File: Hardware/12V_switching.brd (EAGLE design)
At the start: 39.4 x 50.9 mm, 10 parts, among them IC5 LM2576D2TR4-012G, J1 POWERPOLE_POWER45A, J2 POWERPOLE_POWER45A

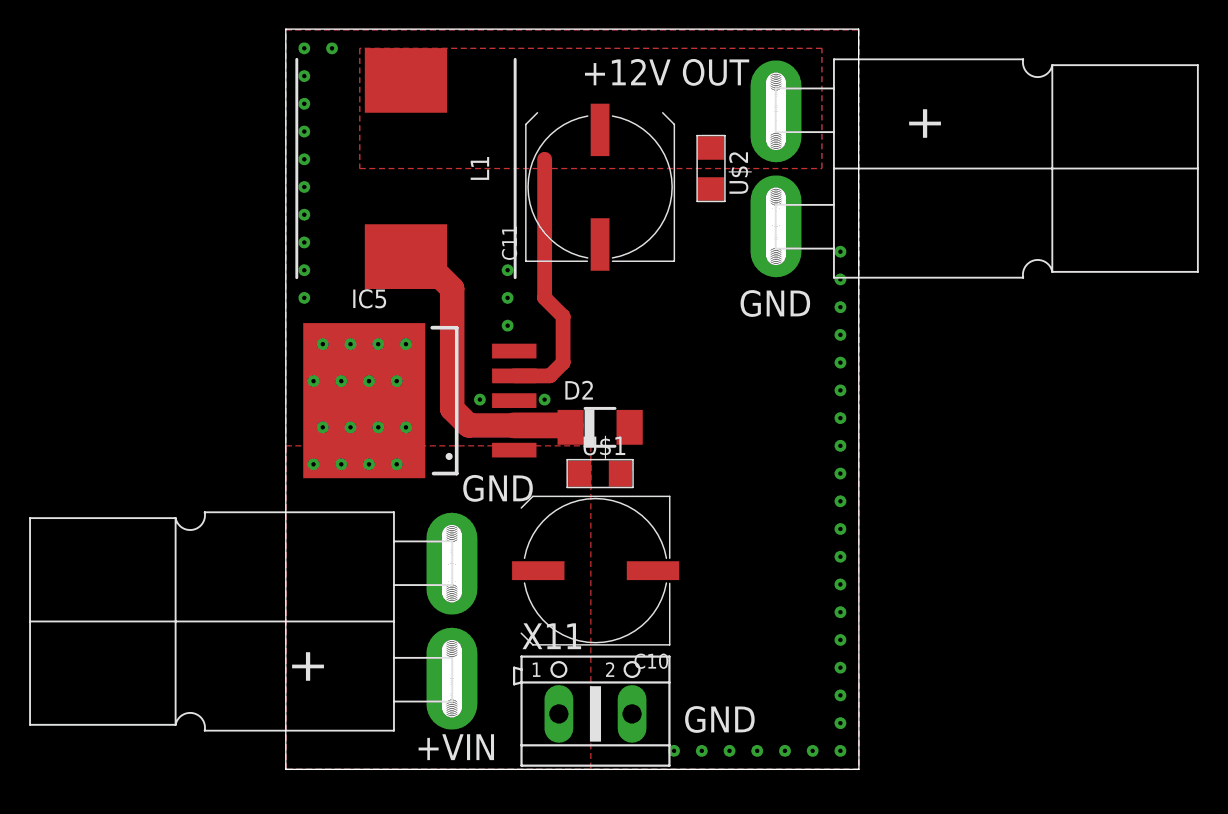
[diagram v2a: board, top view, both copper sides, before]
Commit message: Fix dimention layer on  RTI-Dome-eth.brd, added MPN on all component for mouser.
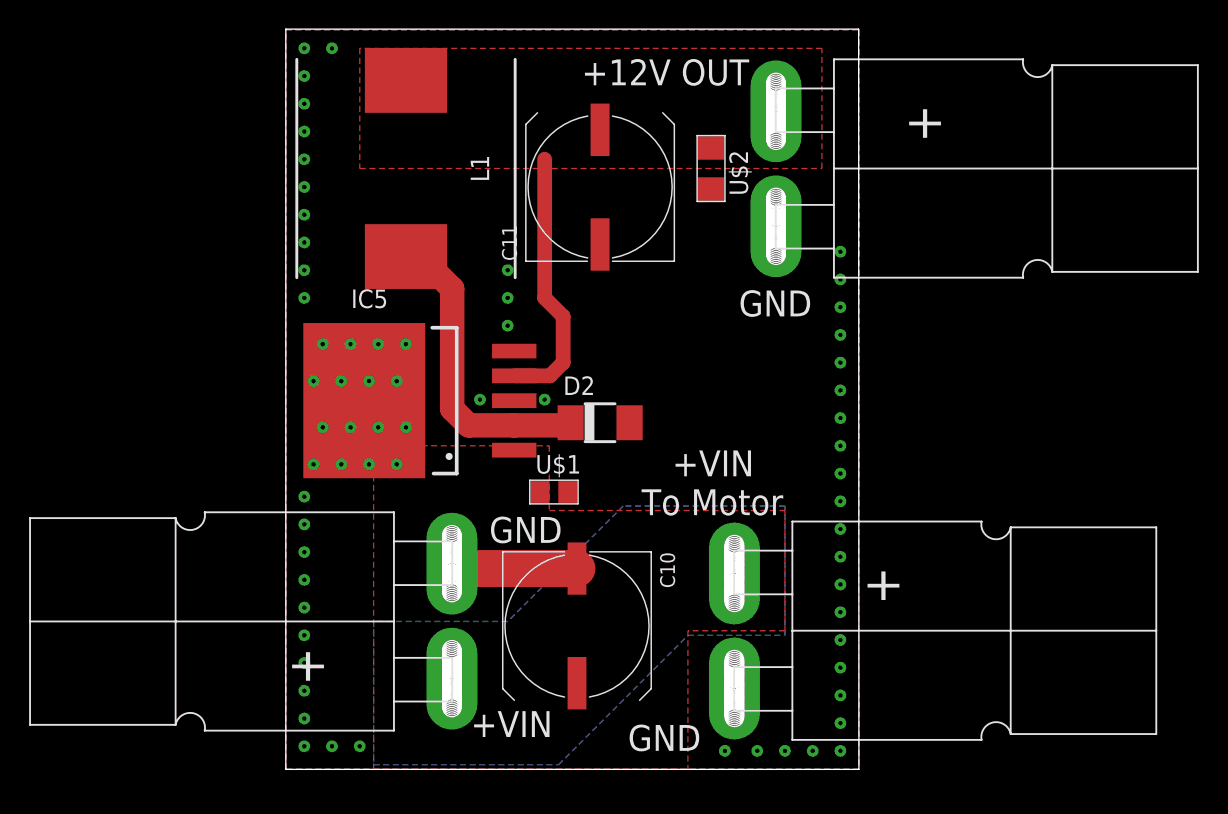
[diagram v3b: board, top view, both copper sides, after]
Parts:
- removed X11: (no value), con-ptr500:AK500/2
- added J3: POWERPOLE_POWER45A, powerpoles:POWERPOLE_PAIR_45A
- U$1: device rti:C1206 -> rti:C0805
- moved C10 4.02 mm to (20.0, 9.84), turned to 270 degrees
- moved U$1 3.42 mm to (18.4, 19.1)
- moved D2 0.32 mm to (21.6, 23.8)
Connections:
- new net V+: J3.RED
- net +VIN: no longer X11.1
- net GND: now also J3.BLACK; no longer X11.2
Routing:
- net GND: track 0.00 -> 8.93 mm, vias 57 -> 67
- added copper zone on layer 16, net +VIN
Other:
- board text added: "+VIN To Motor"
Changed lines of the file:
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@@
 <wire x1="39.35" y1="50.851" x2="0" y2="50.851" width="0" layer="20"/>
 <wire x1="0" y1="50.851" x2="0" y2="0" width="0" layer="20"/>
-<text x="8.89" y="0.635" size="1.778" layer="25">+VIN</text>
-<text x="12.065" y="18.415" size="1.778" layer="25">GND</text>
+<text x="12.7" y="2.2225" size="1.778" layer="25">+VIN</text>
+<text x="13.97" y="15.5575" size="1.778" layer="25">GND</text>
 <text x="31.115" y="31.115" size="1.778" layer="25">GND</text>
 <text x="20.32" y="46.99" size="1.778" layer="25">+12V OUT</text>
-<text x="27.305" y="2.54" size="1.778" layer="25">GND</text>
+<text x="23.495" y="1.27" size="1.778" layer="25">GND</text>
+<text x="24.4475" y="17.4625" size="1.778" layer="21">   +VIN
+To Motor</text>
 </plain>
 <attributes>
@@
 </autorouter>
 <elements>
-<element name="C10" library="rcl" package="UD-10X10_NICHICON" value="100uF" x="21.2725" y="13.6525" rot="R180"/>
+<element name="C10" library="rcl" package="UD-10X10_NICHICON" value="100uF" x="20.0025" y="9.8425" rot="R270"/>
 <element name="C11" library="rcl" package="UD-10X10_NICHICON" value="1000uF" x="21.59" y="40.005" rot="R90"/>
-<element name="D2" library="diode" package="DO-214AC" value="SAC32" x="21.59" y="23.495"/>
+<element name="D2" library="diode" package="DO-214AC" value="SAC32" x="21.59" y="23.8125"/>
 <element name="IC5" library="LM2576" package="TO263-5" value="LM2576D2TR4-012G" x="6.985" y="25.4" rot="R90">
 <attribute name="MOUSER_PART_NUMBER" value="863-LM2576D2TR4-012G" x="6.985" y="25.4" size="1.778" layer="27" rot="R90" display="off"/>
@@
 <attribute name="DESCRIPTION" value="Fixed Inductors MSS1583 SMT Power 0.103Ohms 100uH" x="8.255" y="41.275" size="1.778" layer="27" rot="R90" display="off"/>
 </element>
-<element name="U$1" library="rti" package="C1206" value="47uF" x="21.59" y="20.32"/>
+<element name="U$1" library="rti" package="C0805" value="47uF" x="18.415" y="19.05"/>
 <element name="U$2" library="rti" package="C1206" value="47uF" x="29.21" y="41.275" rot="R270"/>
 <element name="J1" library="powerpoles" package="POWERPOLE_PAIR_45A" value="POWERPOLE_POWER45A" x="11.43" y="10.16" rot="R90"/>
 <element name="J2" library="powerpoles" package="POWERPOLE_PAIR_45A" value="POWERPOLE_POWER45A" x="33.655" y="41.275" rot="R270"/>
-<element name="X11" library="con-ptr500" package="AK500/2" value="" x="21.2725" y="3.81">
-<attribute name="OC_NEWARK" value="unknown" x="21.2725" y="3.81" size="1.778" layer="27" display="off"/>
-<attribute name="MPN" value="" x="21.2725" y="3.81" size="1.778" layer="27" display="off"/>
-<attribute name="MF" value="" x="21.2725" y="3.81" size="1.778" layer="27" display="off"/>
-<attribute name="OC_FARNELL" value="unknown" x="21.2725" y="3.81" size="1.778" layer="27" display="off"/>
-</element>
+<element name="J3" library="powerpoles" package="POWERPOLE_PAIR_45A" value="POWERPOLE_POWER45A" x="30.7975" y="9.525" rot="R270"/>
 </elements>
 <signals>
@@
 <contactref element="D2" pad="A"/>
 <contactref element="C11" pad="-"/>
-<polygon width="0.4064" layer="16" thermals="no">
+<polygon width="0.4064" layer="16" thermals="no" rank="2">
 <vertex x="0" y="0"/>
 <vertex x="0" y="50.8"/>
@@
 <contactref element="J2" pad="BLACK"/>
 <contactref element="J1" pad="BLACK"/>
-<contactref element="X11" pad="2"/>
+<via x="3.175" y="1.5875" extent="1-16" drill="0.3" diameter="0.8128"/>
+<via x="5.08" y="1.5875" extent="1-16" drill="0.3" diameter="0.8128"/>
+<via x="30.1625" y="1.27" extent="1-16" drill="0.3" diameter="0.8128"/>
+<via x="32.385" y="1.27" extent="1-16" drill="0.3" diameter="0.8128"/>
 <via x="34.29" y="1.27" extent="1-16" drill="0.3" diameter="0.8128"/>
-<via x="32.385" y="1.27" extent="1-16" drill="0.3" diameter="0.8128"/>
-<via x="30.48" y="1.27" extent="1-16" drill="0.3" diameter="0.8128"/>
-<via x="28.575" y="1.27" extent="1-16" drill="0.3" diameter="0.8128"/>
-<via x="26.67" y="1.27" extent="1-16" drill="0.3" diameter="0.8128"/>
+<contactref element="J3" pad="BLACK"/>
+<wire x1="20.0025" y1="13.7925" x2="11.41" y2="13.7925" width="2.54" layer="1"/>
+<wire x1="11.41" y1="13.7925" x2="11.41" y2="14.13" width="2.54" layer="1"/>
+<via x="1.27" y="18.7325" extent="1-16" drill="0.3" diameter="0.8128"/>
+<via x="1.27" y="16.8275" extent="1-16" drill="0.3" diameter="0.8128"/>
+<via x="1.27" y="14.9225" extent="1-16" drill="0.3" diameter="0.8128"/>
+<via x="1.27" y="13.0175" extent="1-16" drill="0.3" diameter="0.8128"/>
+<via x="1.27" y="11.1125" extent="1-16" drill="0.3" diameter="0.8128"/>
+<via x="1.27" y="9.2075" extent="1-16" drill="0.3" diameter="0.8128"/>
+<via x="1.27" y="7.3025" extent="1-16" drill="0.3" diameter="0.8128"/>
+<via x="1.27" y="5.3975" extent="1-16" drill="0.3" diameter="0.8128"/>
+<via x="1.27" y="3.4925" extent="1-16" drill="0.3" diameter="0.8128"/>
+<via x="1.27" y="1.5875" extent="1-16" drill="0.3" diameter="0.8128"/>
 </signal>
 <signal name="+VIN" class="1">
@@
 <contactref element="C10" pad="+"/>
 <polygon width="0.4064" layer="1" thermals="no">
-<vertex x="0" y="22.225"/>
-<vertex x="20.955" y="22.225"/>
-<vertex x="20.955" y="0"/>
-<vertex x="0" y="0"/>
+<vertex x="6.0325" y="22.225"/>
+<vertex x="18.0975" y="22.225"/>
+<vertex x="18.0975" y="17.78"/>
+<vertex x="34.29" y="17.78"/>
+<vertex x="34.29" y="9.525"/>
+<vertex x="27.6225" y="9.525"/>
+<vertex x="27.6225" y="0"/>
+<vertex x="6.0325" y="0"/>
 </polygon>
 <contactref element="U$1" pad="1"/>
 <contactref element="J1" pad="RED"/>
-<contactref element="X11" pad="1"/>
+<polygon width="0.254" layer="16">
+<vertex x="34.29" y="18.0975"/>
+<vertex x="23.1775" y="18.0975"/>
+<vertex x="15.24" y="10.16"/>
+<vertex x="6.0325" y="10.16"/>
+<vertex x="6.0325" y="0.3175"/>
+<vertex x="18.7325" y="0.3175"/>
+<vertex x="27.6225" y="9.2075"/>
+<vertex x="34.29" y="9.2075"/>
+</polygon>
 </signal>
 <signal name="+12V">
@@
 <contactref element="D2" pad="C"/>
 <contactref element="L1" pad="1"/>
-<wire x1="15.695" y1="23.628" x2="19.565" y2="23.628" width="1.778" layer="1"/>
-<wire x1="19.565" y1="23.628" x2="19.565" y2="23.495" width="1.778" layer="1"/>
 <wire x1="15.695" y1="23.628" x2="12.567" y2="23.628" width="1.6764" layer="1"/>
 <wire x1="12.567" y1="23.628" x2="11.43" y2="24.765" width="1.6764" layer="1"/>
@@
 <wire x1="9.525" y1="34.925" x2="7.285" y2="34.925" width="1.6764" layer="1"/>
 <wire x1="7.285" y1="34.925" x2="8.255" y2="35.225" width="1.6764" layer="1"/>
+<wire x1="15.695" y1="23.628" x2="19.565" y2="23.628" width="1.6764" layer="1"/>
+<wire x1="19.565" y1="23.628" x2="19.565" y2="23.8125" width="1.6764" layer="1"/>
+</signal>
+<signal name="V+">
+<contactref element="J3" pad="RED"/>
 </signal>
 </signals>
@@
 </board>
 </drawing>
+<compatibility>
+<note version="6.3" minversion="6.2.2" severity="warning">
+Since Version 6.2.2 text objects can contain more than one line,
+which will not be processed correctly with this version.
+</note>
+</compatibility>
 </eagle>

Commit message: Change pin mode for better interrupt detection
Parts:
- removed U$1: 47uF, rti:C0805
- C10: value 100uF -> 100uF 100V
- D2: value SAC32 -> SAC34
- IC5: value LM2576D2TR4-012G -> LM2576HVSX-12/NOPB
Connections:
- net +VIN: no longer U$1.1
- net GND: no longer U$1.2
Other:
- board text added: "+VOUT To Motor"
- board text removed: "+VIN To Motor"
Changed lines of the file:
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@@
 <text x="20.32" y="46.99" size="1.778" layer="25">+12V OUT</text>
 <text x="23.495" y="1.27" size="1.778" layer="25">GND</text>
-<text x="24.4475" y="17.4625" size="1.778" layer="21">   +VIN
+<text x="27.6225" y="17.78" size="1.778" layer="21"> +VOUT
 To Motor</text>
 </plain>
@@
 </autorouter>
 <elements>
-<element name="C10" library="rcl" package="UD-10X10_NICHICON" value="100uF" x="20.0025" y="9.8425" rot="R270"/>
+<element name="C10" library="rcl" package="UD-10X10_NICHICON" value="100uF 100V" x="20.0025" y="9.8425" rot="R270"/>
 <element name="C11" library="rcl" package="UD-10X10_NICHICON" value="1000uF" x="21.59" y="40.005" rot="R90"/>
-<element name="D2" library="diode" package="DO-214AC" value="SAC32" x="21.59" y="23.8125"/>
-<element name="IC5" library="LM2576" package="TO263-5" value="LM2576D2TR4-012G" x="6.985" y="25.4" rot="R90">
-<attribute name="MOUSER_PART_NUMBER" value="863-LM2576D2TR4-012G" x="6.985" y="25.4" size="1.778" layer="27" rot="R90" display="off"/>
+<element name="D2" library="diode" package="DO-214AC" value="SAC34" x="21.59" y="23.8125"/>
+<element name="IC5" library="LM2576" package="TO263-5" value="LM2576HVSX-12/NOPB" x="6.985" y="25.4" rot="R90">
+<attribute name="MOUSER_PART_NUMBER" value=" LM2576HVSX-12/NOPB" x="6.985" y="25.4" size="1.778" layer="27" rot="R90" display="off"/>
 <attribute name="MANUFACTURER_NAME" value="ON Semiconductor" x="6.985" y="25.4" size="1.778" layer="27" rot="R90" display="off"/>
 <attribute name="MOUSER_PRICE-STOCK" value="https://www.mouser.com/Search/Refine.aspx?Keyword=863-LM2576D2TR4-5G" x="6.985" y="25.4" size="1.778" layer="27" rot="R90" display="off"/>
@@
 <attribute name="MANUFACTURER_PART_NUMBER" value="LM2576D2TR4-012G " x="6.985" y="25.4" size="1.778" layer="27" rot="R90" display="off"/>
 <attribute name="DESCRIPTION" value="Voltage Regulators - Switching Regulators 5V 3A Buck PWM" x="6.985" y="25.4" size="1.778" layer="27" rot="R90" display="off"/>
-<attribute name="MPN" value="LM2576D2TR4-012G " x="6.985" y="25.4" size="1.778" layer="27" rot="R90" display="off"/>
+<attribute name="MPN" value=" LM2576HVSX-12/NOPB" x="6.985" y="25.4" size="1.778" layer="27" rot="R90" display="off"/>
 </element>
 <element name="L1" library="MSS1583-104KEB" package="INDPM150150X860N" value="MSS1583-104KEB" x="8.255" y="41.275" rot="R90">
@@
 <attribute name="DESCRIPTION" value="Fixed Inductors MSS1583 SMT Power 0.103Ohms 100uH" x="8.255" y="41.275" size="1.778" layer="27" rot="R90" display="off"/>
 </element>
-<element name="U$1" library="rti" package="C0805" value="47uF" x="18.415" y="19.05"/>
 <element name="U$2" library="rti" package="C1206" value="47uF" x="29.21" y="41.275" rot="R270"/>
 <element name="J1" library="powerpoles" package="POWERPOLE_PAIR_45A" value="POWERPOLE_POWER45A" x="11.43" y="10.16" rot="R90"/>
@@
 <vertex x="39.37" y="0"/>
 </polygon>
-<contactref element="U$1" pad="2"/>
 <contactref element="U$2" pad="2"/>
 <via x="17.78" y="25.4" extent="1-16" drill="0.3" diameter="0.8128"/>
@@
 <vertex x="6.0325" y="0"/>
 </polygon>
-<contactref element="U$1" pad="1"/>
 <contactref element="J1" pad="RED"/>
 <polygon width="0.254" layer="16">

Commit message: Fix a non connected network on the board... the motor VOut .. :(
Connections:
- removed net V+: J3.RED
- net +VIN: now also J3.RED
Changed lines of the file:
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@@
 <vertex x="34.29" y="9.2075"/>
 </polygon>
+<contactref element="J3" pad="RED"/>
 </signal>
 <signal name="+12V">
@@
 <wire x1="19.565" y1="23.628" x2="19.565" y2="23.8125" width="1.6764" layer="1"/>
 </signal>
-<signal name="V+">
-<contactref element="J3" pad="RED"/>
-</signal>
 </signals>
